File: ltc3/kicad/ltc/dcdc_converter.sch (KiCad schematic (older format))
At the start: 50 parts, among them P201 MicroFit header, P202 JST PH header, P203 JST PH housing, P204 PIN_HEAD_1x2, P205 PIN_HEAD_1x2, P206 PIN_HEAD_1x2, Q202 BSS138, Q203 BSS138, SW201 SPST, U201 PTN78020W, U202 LTC2991, U203 PTN78020H, U204 PTN78020H

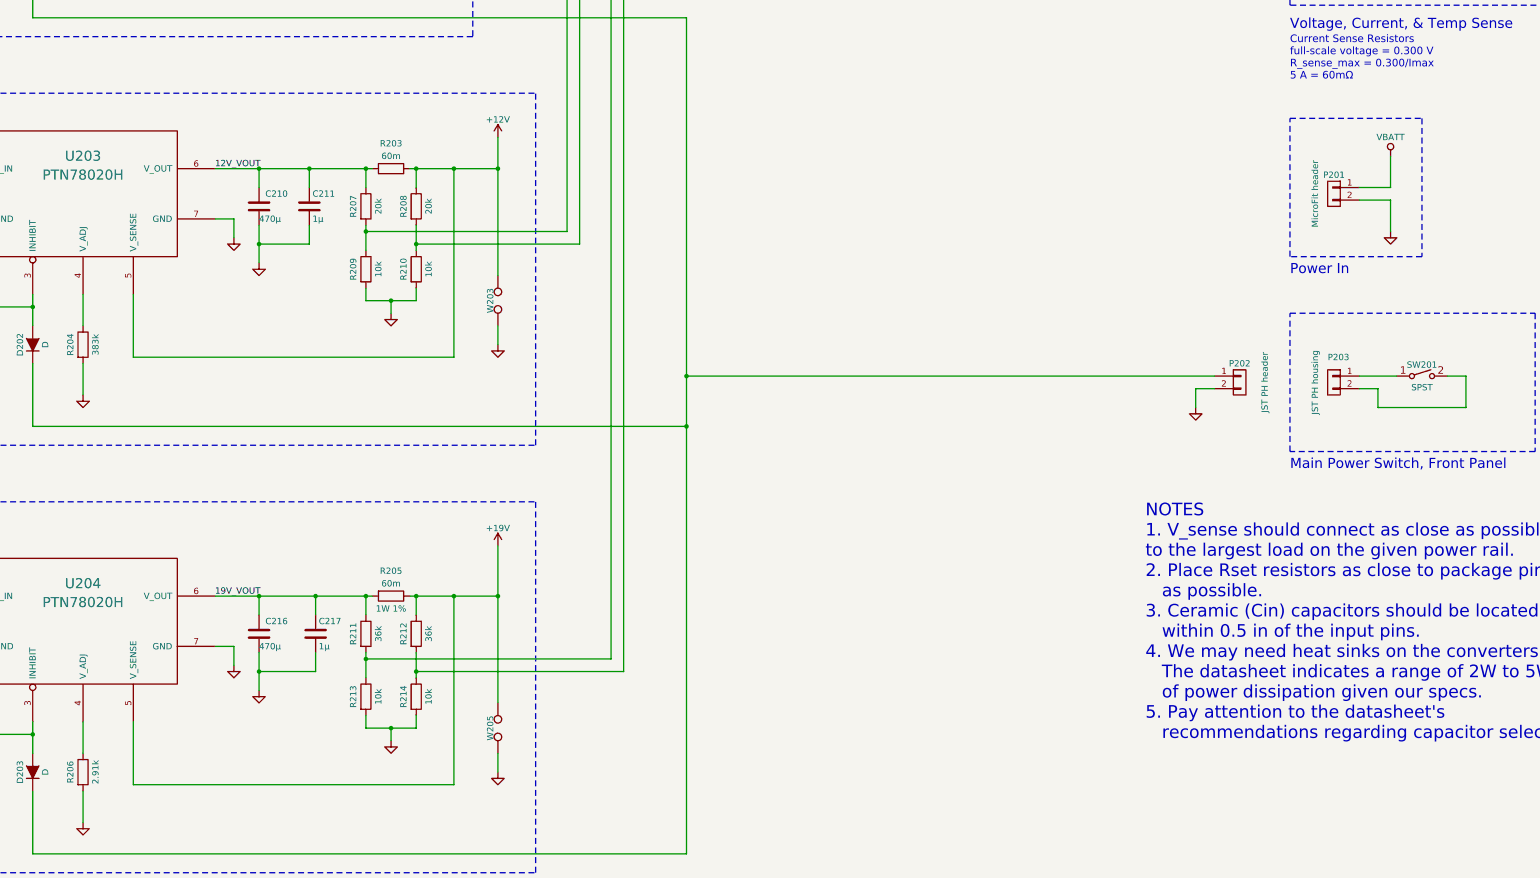
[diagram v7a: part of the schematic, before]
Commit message: LTC3: More BOM work, mostly on the LTC proper.
Plus a few minor tweaks to the charge controller and cell protection
BOMs that should not impact PCB layout.

Nearly finished with LTC BOM.
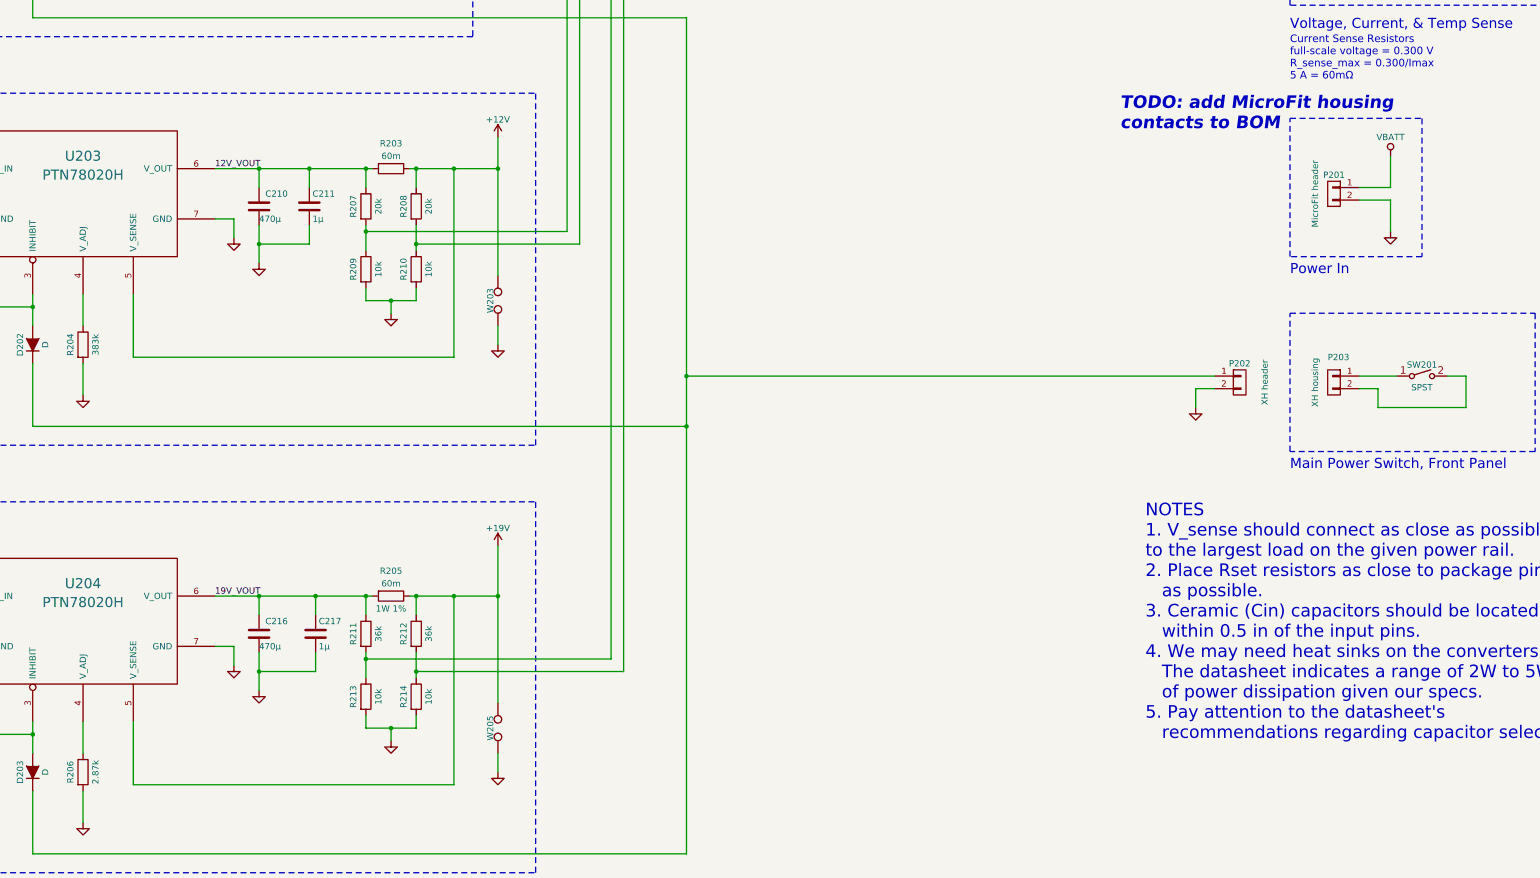
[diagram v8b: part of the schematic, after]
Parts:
- C201, C204, C211, C217: Mfg_Description (none) -> 100V X7S 10%; Mfg_Name - -> TDK; Mfg_PN - -> CGA4J3X7S2A105K125AB
- C202: footprint Capacitors_SMD:C_0805 -> Capacitors_SMD:C_1210; Mfg_Description (none) -> 100V X7R 10%; Mfg_Name - -> Murata; Mfg_PN - -> GRM32ER72A225KA35L
- C203, C210, C216: footprint Capacitors_ThroughHole:C_Radial_D10_L25_P5 -> Capacitors_ThroughHole:C_Radial_D16_L25_P7.5; Mfg_Description (none) -> 100V 20%; Mfg_Name - -> Nichicon; Mfg_PN - -> UVZ2A471MHD
- C205: Mfg_Description (none) -> 100V X7R 10%; Mfg_Name - -> Murata; Mfg_PN - -> GCM21BR72A104KA37L
- C206, C207, C208, C209, C212, C213, C214, C215: Mfg_Description (none) -> 100V X7R 10%; Mfg_Name - -> Murata; Mfg_PN - -> GRM219R72A472KA01D
- D201, D202, D203: footprint (none) -> ~; Mfg_Description (none) -> -; Mfg_Name (none) -> -; Mfg_PN (none) -> -; Note (none) -> -; Spec (none) -> -
- P201, U202: Mfg_Description (none) -> -
- P202: value JST PH header -> XH header; footprint Connectors_JST:JST_PH_B2B-PH-K_09x2.00mm_Straight -> ~; Mfg_Description (none) -> -; Mfg_PN JST B2B-PH-K-S -> -; Note (none) -> -; Spec (none) -> -
- P203: value JST PH housing -> XH housing; footprint (none) -> ~; Mfg_Description (none) -> -; Mfg_PN PHR-2 -> -; Note (none) -> -; Spec (none) -> -
- P204, P205, P206: footprint (none) -> Pin_Headers:Pin_Header_Straight_1x02; Mfg_Description (none) -> -
- Q202, Q203: Mfg_Description (none) -> -; Spec (none) -> -
- R201, R203, R205: footprint LTC3:CST0612 -> Resistors_SMD:R_2512; Mfg_Description (none) -> 1% 2W; Mfg_Name Bourns -> Yageo; Mfg_PN CST0612-FX-R060-E -> PE2512FKE7W0R06L
- R202: Mfg_Description (none) -> 1% 1/8W; Mfg_Name - -> Yageo; Mfg_PN - -> RC0805FR-0721KL
- R204: Mfg_Description (none) -> 1% 1/8W; Mfg_Name - -> Yageo; Mfg_PN - -> RC0805FR-07383KL
- R206: value 2.91k -> 2.87k; Mfg_Description (none) -> 1% 1/8W 100ppm; Mfg_Name - -> Panasonic; Mfg_PN - -> ERJ-6ENF2871V; Note - -> datasheet-spec’d 2.91k is unavailable
- R207, R208: footprint (none) -> Resistors_SMD:R_0805; Mfg_Description (none) -> 1% 1/8W; Mfg_Name (none) -> Yageo; Mfg_PN (none) -> RC0805FR-0720KL; Note (none) -> -; Spec (none) -> -
- R209, R210, R213, R214: footprint (none) -> Resistors_SMD:R_0805; Mfg_Description (none) -> 1% 1/8W; Mfg_Name (none) -> Yageo; Mfg_PN (none) -> RC0805FR-0710KL; Note (none) -> -; Spec (none) -> -
- R211, R212: footprint (none) -> Resistors_SMD:R_0805; Mfg_Description (none) -> 1% 1/8W; Mfg_Name (none) -> Yageo; Mfg_PN (none) -> RC0805FR-0736KL; Note (none) -> -; Spec (none) -> -
- SW201: footprint (none) -> ~; Mfg_Description (none) -> -; Note - -> OFF-BOARD
- U201: Mfg_Description (none) -> REG SW 2.5-12.6V 6A; Mfg_Name (none) -> Texas Instruments; Mfg_PN (none) -> PTN78020WAH; Note (none) -> -; Spec (none) -> -
- U203, U204: Mfg_Description (none) -> REG SW 11.85-22V 6A; Mfg_Name (none) -> Texas Instruments; Mfg_PN (none) -> PTN78020HAH; Note (none) -> -; Spec (none) -> -
- W201, W203, W205: Mfg_Description (none) -> -; Mfg_Name (none) -> -; Mfg_PN (none) -> -; Note (none) -> -; Spec (none) -> -
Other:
- note added: "TODO: add MicroFit housing\ncontacts to BOM"
